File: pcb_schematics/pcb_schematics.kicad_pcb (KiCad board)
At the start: 2 copper layers, 100 x 100 mm, 71 parts, among them J1 CUE_SJ1-352XNG, J2 Conn_01x01_Pin, J3 Conn_01x05, J4 Conn_01x05, J5 Conn_01x05, SW1 SW_Push, U1 RPi_Pico_TH, U2 RDA5807M_Module, U3 LM386, U4 LM386

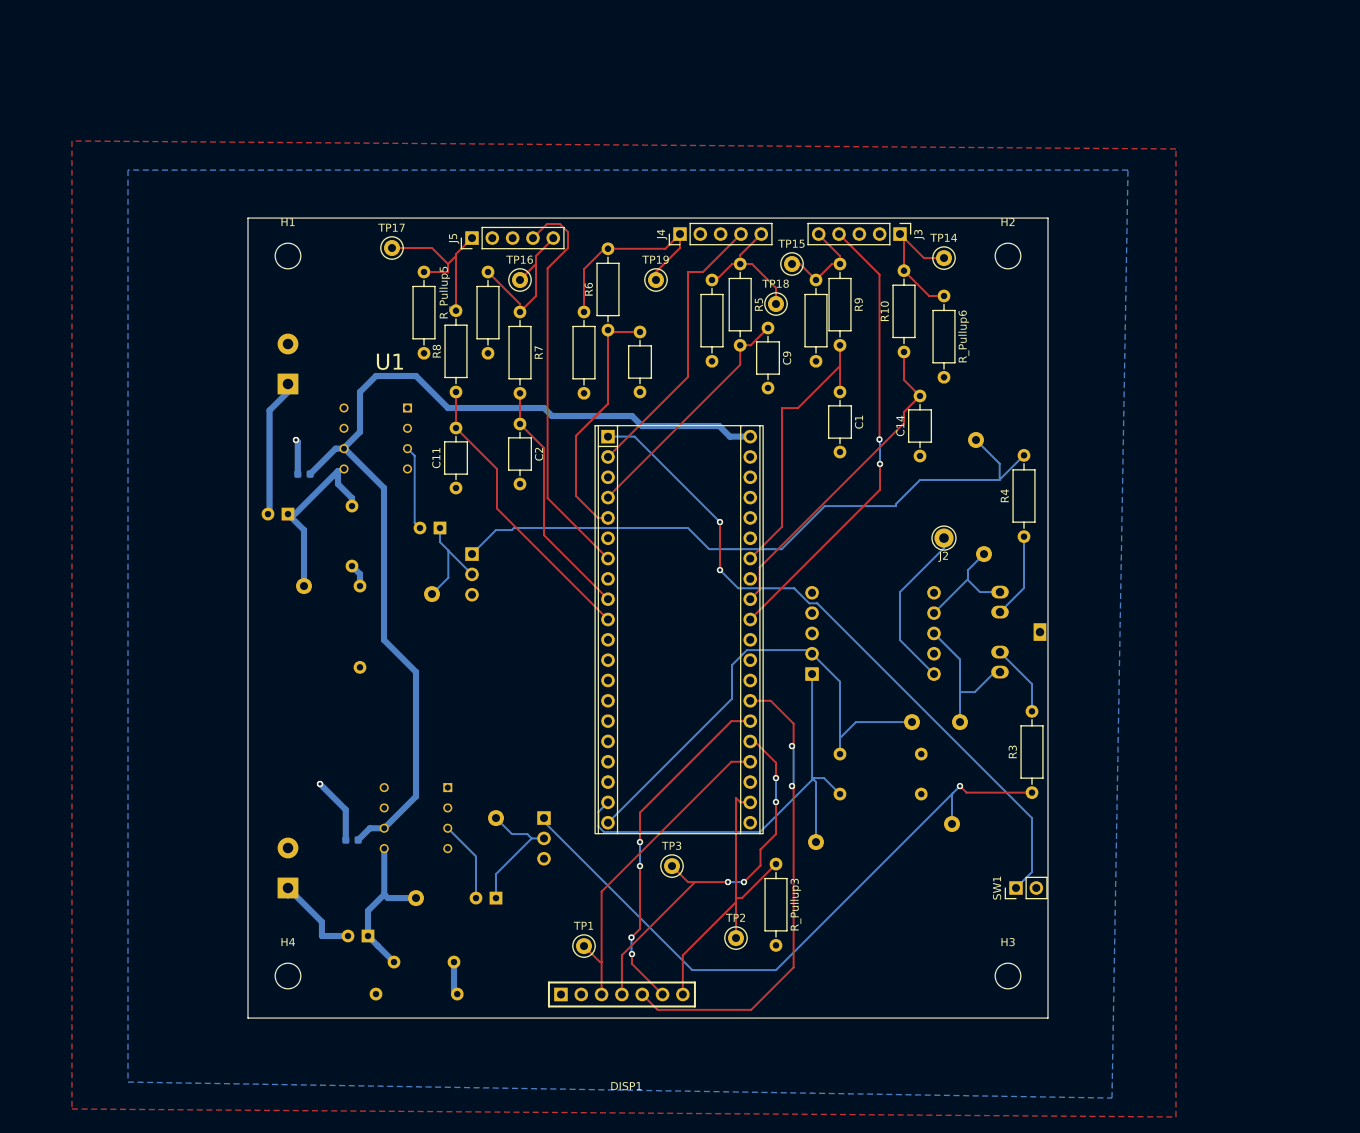
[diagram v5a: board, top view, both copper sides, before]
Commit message: made changes based on changes requested
Fix iteration 2
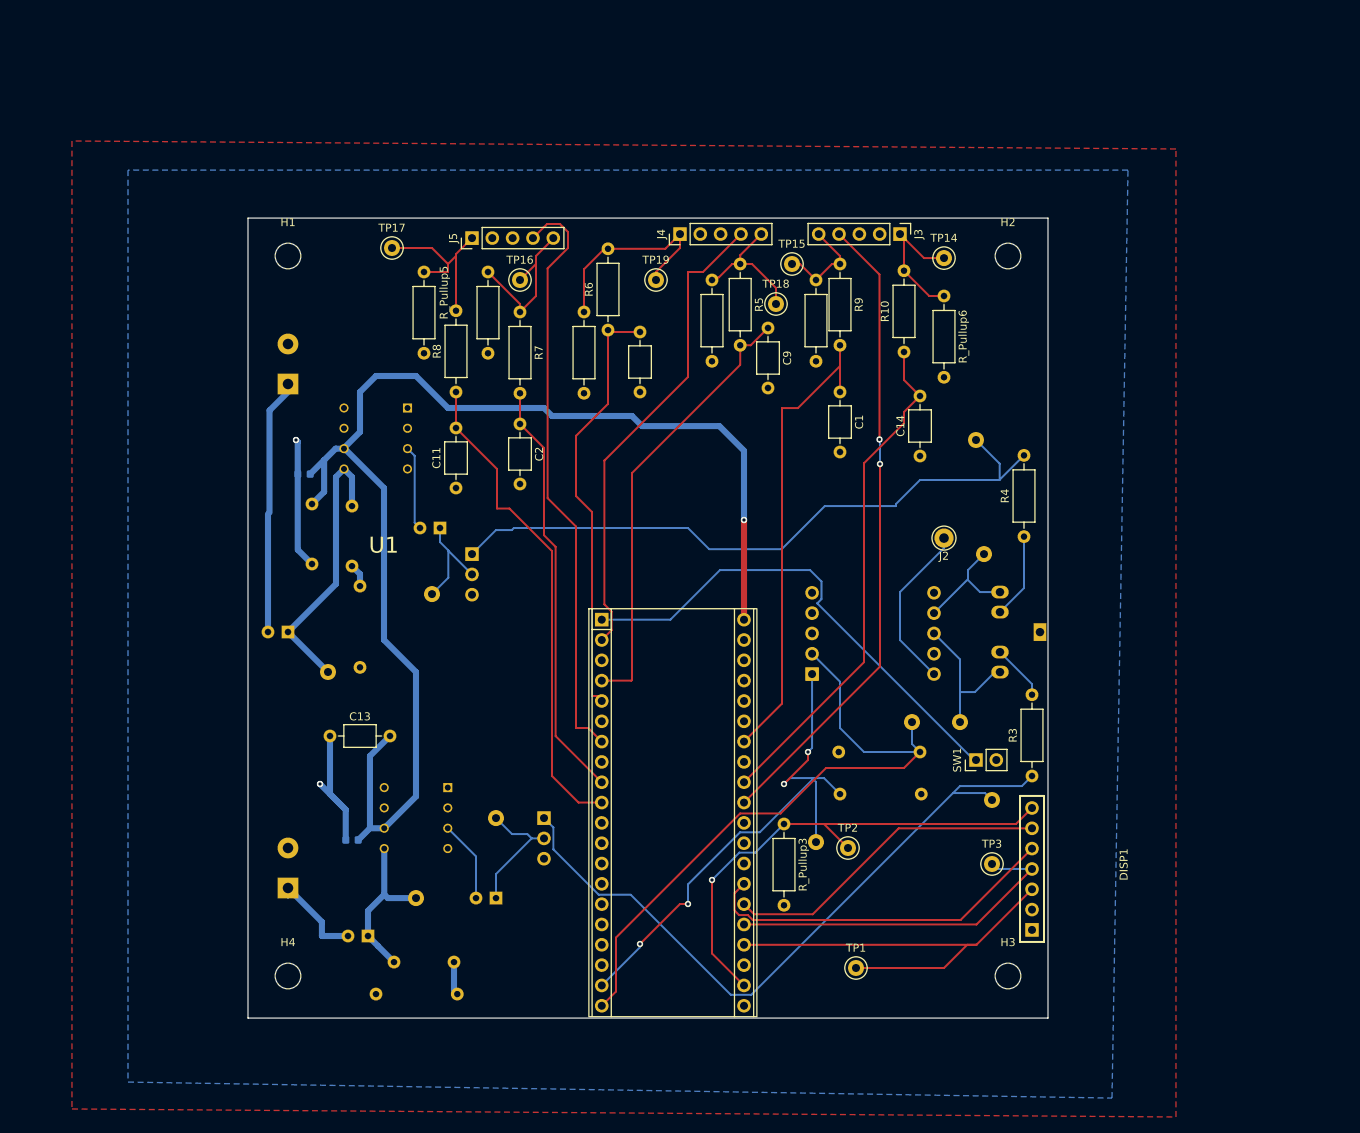
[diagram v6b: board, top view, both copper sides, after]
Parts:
- added C12: 0.1 µF, Capacitor_THT:C_Axial_L3.8mm_D2.6mm_P7.50mm_Horizontal, B.Cu at (103.0, 86.5)
- added C13: 0.1 µF, Capacitor_THT:C_Axial_L3.8mm_D2.6mm_P7.50mm_Horizontal, F.Cu at (105.2, 108.0)
- moved DISP1 105.3 mm to (224.9, 142.4), turned to 90 degrees
- moved TP3 40.0 mm to (188.0, 124.0)
- moved TP1 34.1 mm to (171.0, 137.0)
- moved U1 22.9 mm to (148.1, 117.6)
- moved TP2 18.0 mm to (170.0, 122.0)
- moved SW1 16.8 mm to (186.0, 111.0)
- moved C3 14.7 mm to (100.0, 95.0)
- moved TP9 11.2 mm to (105.0, 100.0)
- moved Rpullup1 10.0 mm to (179.0, 110.0), turned to 180 degrees
- moved TP13 5.83 mm to (188.0, 116.0)
- moved R_Pullup3 5.11 mm to (162.0, 119.0)
- moved R3 2.08 mm to (193.0, 113.0)
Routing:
- net +5V: track 123.1 -> 162.8 mm, vias 0 -> 1
- net /ROT1B: track 30.1 -> 55.6 mm
- net /ROT2B: track 36.6 -> 61.5 mm
- net /SW1: track 85.8 -> 61.9 mm, vias 2 -> 0
- net /SW2: track 35.8 -> 59.8 mm
- net /SW4: track 50.5 -> 74.0 mm
- net /ROT3A: track 35.7 -> 58.9 mm
- net /ROT3B: track 40.5 -> 63.7 mm
- net /SW3: track 57.1 -> 80.3 mm
- net /ROT2A: track 30.3 -> 52.9 mm
- net /ROT1A: track 31.6 -> 53.8 mm
- net GND: track 13.7 -> 35.7 mm
- net /CS: track 41.1 -> 63.1 mm, vias 0 -> 1
- net /I2CSCK: track 62.9 -> 83.6 mm
- net Net-(C3-Pad2): track 17.3 -> 32.0 mm
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
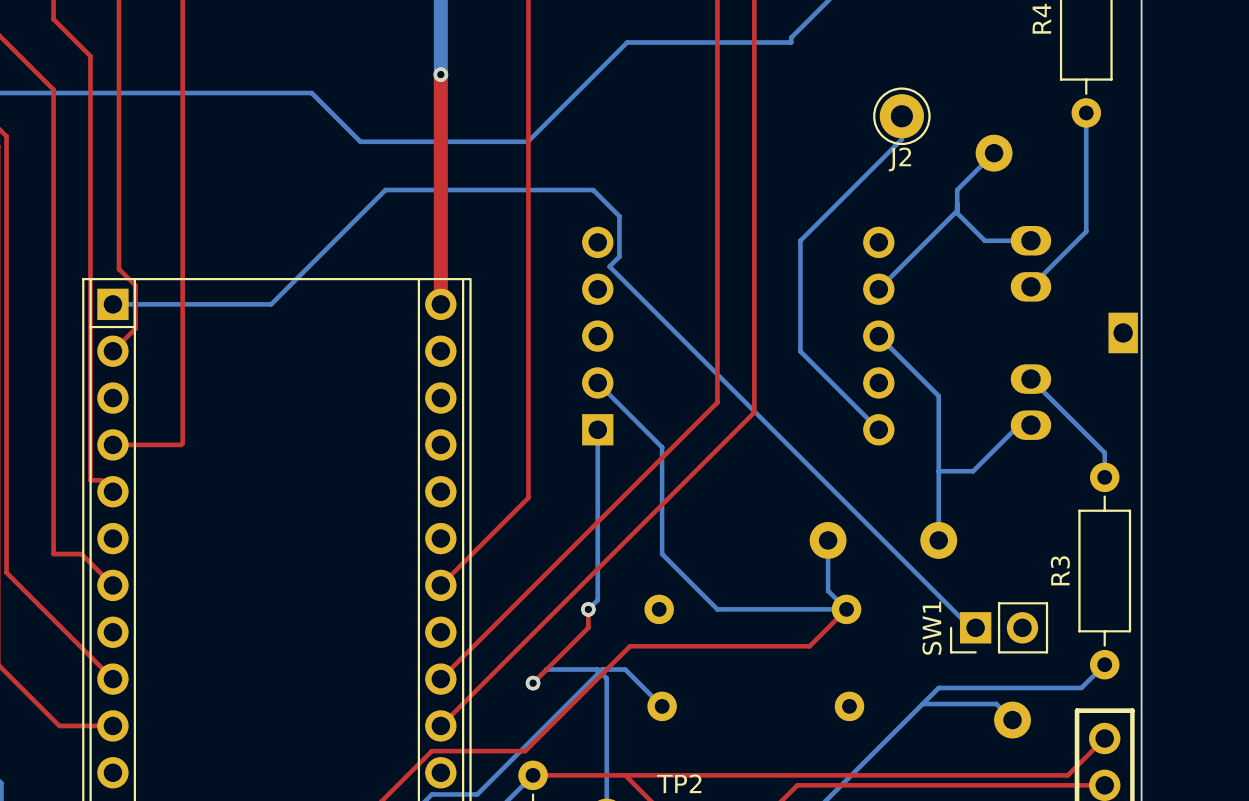
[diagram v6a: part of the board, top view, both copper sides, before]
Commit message: Submitted to JLCPCB
Modification with pcb_schematics being the final version.
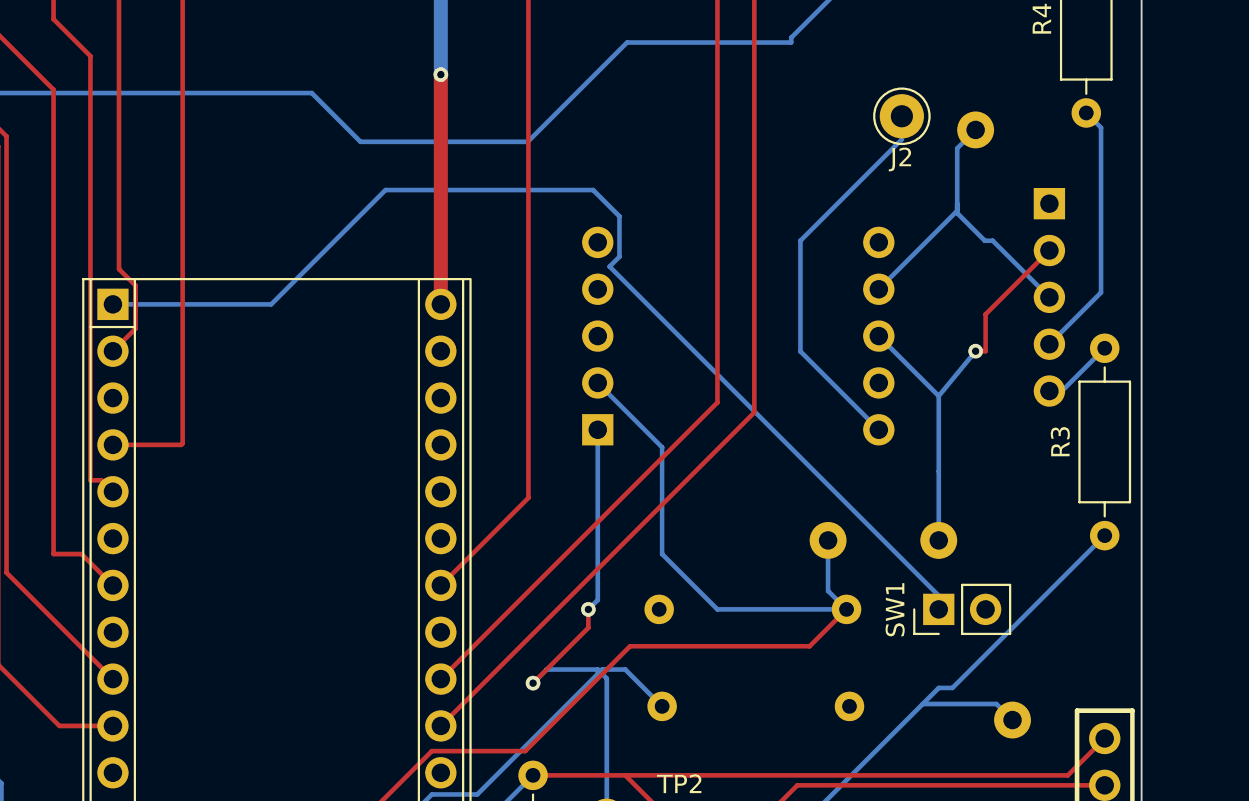
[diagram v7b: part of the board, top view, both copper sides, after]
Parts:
- J1: footprint ECE:CUE_SJ1-352XNG -> Connector_PinHeader_2.54mm:PinHeader_1x05_P2.54mm_Vertical
- moved J1 8.07 mm to (190.0, 88.0)
- moved R3 7.00 mm to (193.0, 106.0)
- moved SW1 2.24 mm to (184.0, 110.0)
- moved TP11 1.61 mm to (186.0, 84.0)
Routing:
- net /LOUT: track 18.3 -> 23.0 mm, vias 0 -> 1
- net /RSpeaker: track 10.9 -> 14.0 mm
- net /ROUT: track 15.1 -> 18.2 mm
- net /LSpeaker: track 6.99 -> 3.96 mm
- net Net-(R3-Pad1): track 88.8 -> 91.7 mm
- net /SW1: track 61.9 -> 59.9 mm
